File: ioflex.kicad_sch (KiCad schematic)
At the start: 2 parts, among them CN12 DF40C-50DS-0.4V, CN13 DF40C-50DS-0.4V

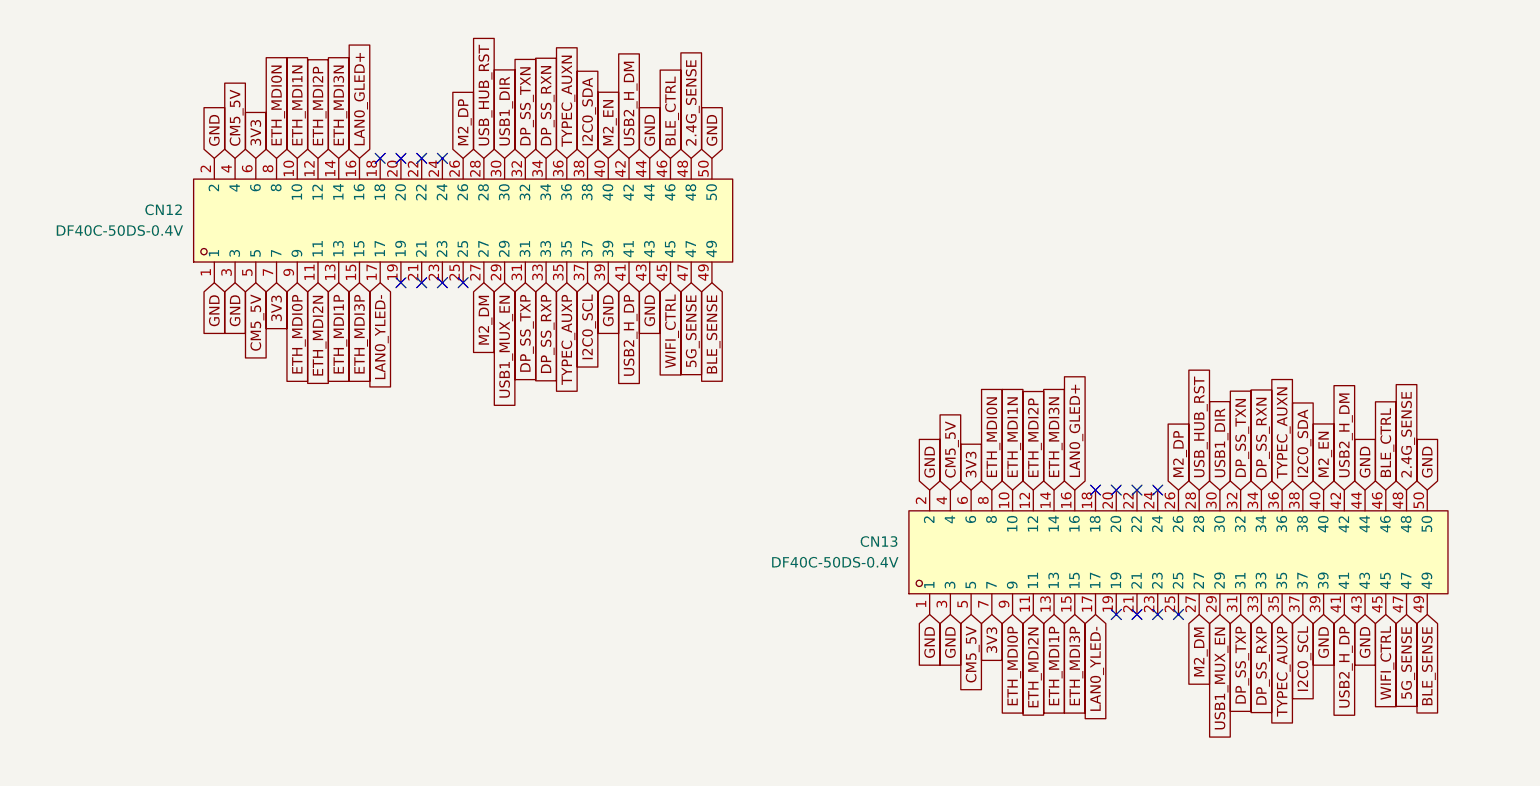
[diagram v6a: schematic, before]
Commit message: imported footprints and 3d models, replaced obsolete components, finished schematic audit, wired new usb hub and flash chip + more, removed stale nets
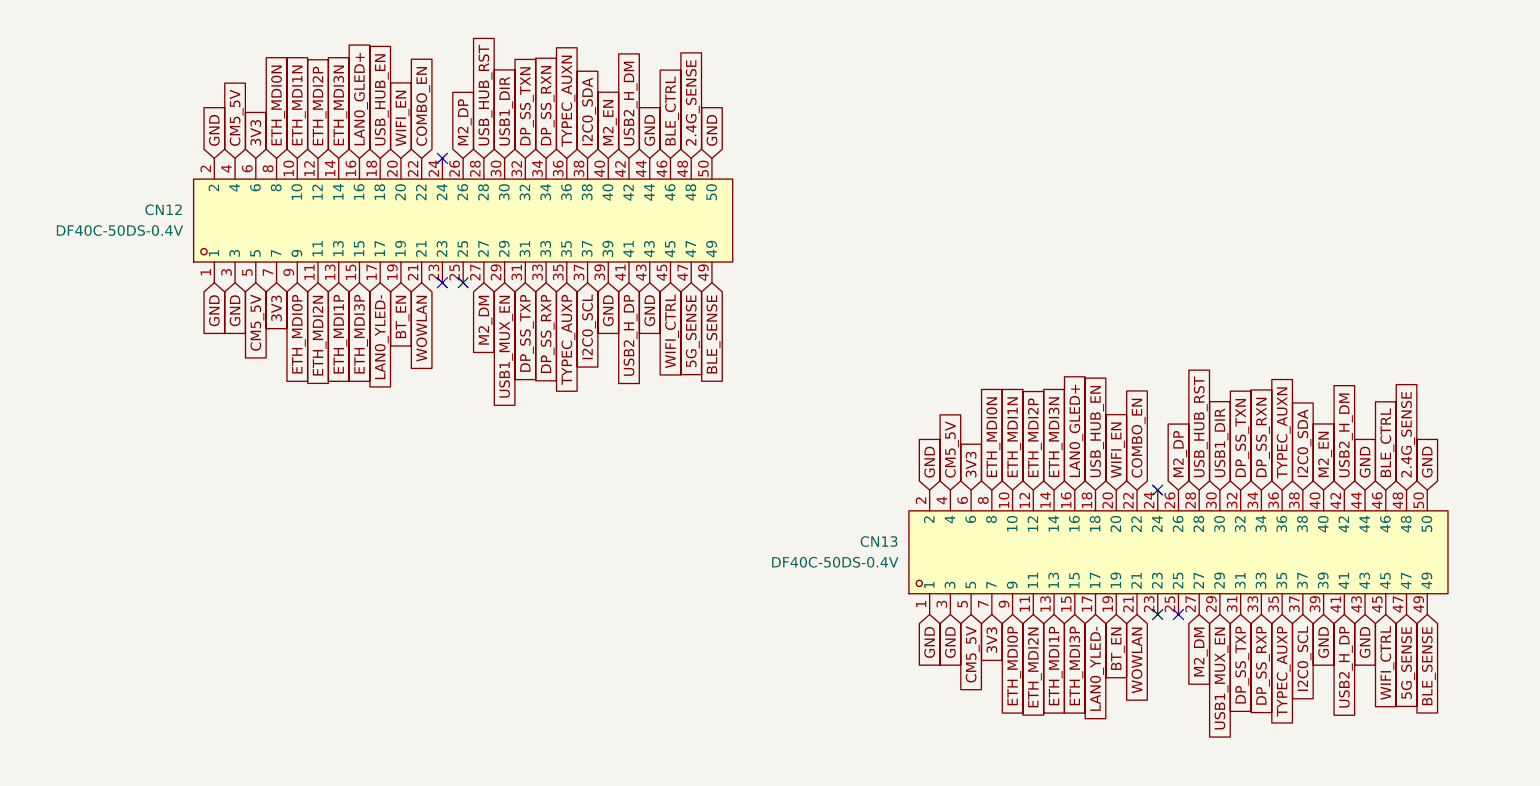
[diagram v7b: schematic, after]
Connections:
- net USB_HUB_EN: now reaches CN13.18
- net USB_HUB_EN: now also CN12.18
- net BT_EN: now reaches CN13.19
- net BT_EN: now also CN12.19
- net WIFI_EN: now reaches CN13.20
- net WIFI_EN: now also CN12.20
- net WOWLAN: now reaches CN13.21
- net WOWLAN: now also CN12.21
- net COMBO_EN: now reaches CN13.22
- net COMBO_EN: now also CN12.22
- no-connect marks 16 -> 6
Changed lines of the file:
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@@
 	(paper "A5")
 	(no_connect
-		(at 60.96 29.21)
-	)
-	(no_connect
-		(at 148.59 85.09)
-	)
-	(no_connect
-		(at 60.96 44.45)
-	)
-	(no_connect
-		(at 55.88 29.21)
-	)
-	(no_connect
 		(at 153.67 85.09)
 	)
@@
 	)
 	(no_connect
-		(at 58.42 29.21)
+		(at 63.5 29.21)
 	)
 	(no_connect
-		(at 146.05 69.85)
+		(at 151.13 85.09)
 	)
 	(no_connect
-		(at 63.5 29.21)
-	)
-	(no_connect
-		(at 146.05 85.09)
-	)
-	(no_connect
-		(at 148.59 69.85)
-	)
-	(no_connect
-		(at 58.42 44.45)
+		(at 66.04 44.45)
 	)
 	(no_connect
 		(at 63.5 44.45)
 	)
-	(no_connect
-		(at 143.51 69.85)
-	)
-	(no_connect
-		(at 66.04 44.45)
-	)
-	(no_connect
-		(at 151.13 85.09)
-	)
 	(global_label "3V3"
 		(shape input)
@@
 		)
 	)
+	(global_label "USB_HUB_EN"
+		(shape input)
+		(at 143.51 69.85 90)
+		(fields_autoplaced yes)
+		(effects
+			(font
+				(size 1.27 1.27)
+			)
+			(justify left)
+		)
+		(property "Intersheetrefs" "${INTERSHEET_REFS}"
+			(at 143.51 54.7091 90)
+			(hide yes)
+			(show_name no)
+			(do_not_autoplace no)
+			(effects
+				(font
+					(size 1.27 1.27)
+				)
+				(justify left)
+			)
+		)
+	)
 	(global_label "DP_SS_RXP"
 		(shape input)
@@
 		)
 	)
+	(global_label "WIFI_EN"
+		(shape input)
+		(at 58.42 29.21 90)
+		(fields_autoplaced yes)
+		(effects
+			(font
+				(size 1.27 1.27)
+			)
+			(justify left)
+		)
+		(property "Intersheetrefs" "${INTERSHEET_REFS}"
+			(at 58.42 19.0281 90)
+			(hide yes)
+			(show_name no)
+			(do_not_autoplace no)
+			(effects
+				(font
+					(size 1.27 1.27)
+				)
+				(justify left)
+			)
+		)
+	)
 	(global_label "ETH_MDI3N"
 		(shape input)
@@
 		)
 	)
+	(global_label "COMBO_EN"
+		(shape input)
+		(at 148.59 69.85 90)
+		(fields_autoplaced yes)
+		(effects
+			(font
+				(size 1.27 1.27)
+			)
+			(justify left)
+		)
+		(property "Intersheetrefs" "${INTERSHEET_REFS}"
+			(at 148.59 56.7653 90)
+			(hide yes)
+			(show_name no)
+			(do_not_autoplace no)
+			(effects
+				(font
+					(size 1.27 1.27)
+				)
+				(justify left)
+			)
+		)
+	)
 	(global_label "M2_DP"
 		(shape input)
@@
 		)
 	)
+	(global_label "USB_HUB_EN"
+		(shape input)
+		(at 55.88 29.21 90)
+		(fields_autoplaced yes)
+		(effects
+			(font
+				(size 1.27 1.27)
+			)
+			(justify left)
+		)
+		(property "Intersheetrefs" "${INTERSHEET_REFS}"
+			(at 55.88 14.0691 90)
+			(hide yes)
+			(show_name no)
+			(do_not_autoplace no)
+			(effects
+				(font
+					(size 1.27 1.27)
+				)
+				(justify left)
+			)
+		)
+	)
 	(global_label "ETH_MDI0P"
 		(shape input)
@@
 		)
 	)
+	(global_label "BT_EN"
+		(shape input)
+		(at 146.05 85.09 270)
+		(fields_autoplaced yes)
+		(effects
+			(font
+				(size 1.27 1.27)
+			)
+			(justify right)
+		)
+		(property "Intersheetrefs" "${INTERSHEET_REFS}"
+			(at 146.05 93.7599 90)
+			(hide yes)
+			(show_name no)
+			(do_not_autoplace no)
+			(effects
+				(font
+					(size 1.27 1.27)
+				)
+				(justify right)
+			)
+		)
+	)
 	(global_label "I2C0_SCL"
 		(shape input)
@@
 		)
 	)
+	(global_label "COMBO_EN"
+		(shape input)
+		(at 60.96 29.21 90)
+		(fields_autoplaced yes)
+		(effects
+			(font
+				(size 1.27 1.27)
+			)
+			(justify left)
+		)
+		(property "Intersheetrefs" "${INTERSHEET_REFS}"
+			(at 60.96 16.1253 90)
+			(hide yes)
+			(show_name no)
+			(do_not_autoplace no)
+			(effects
+				(font
+					(size 1.27 1.27)
+				)
+				(justify left)
+			)
+		)
+	)
 	(global_label "ETH_MDI0N"
 		(shape input)
@@
 		)
 	)
+	(global_label "WIFI_EN"
+		(shape input)
+		(at 146.05 69.85 90)
+		(fields_autoplaced yes)
+		(effects
+			(font
+				(size 1.27 1.27)
+			)
+			(justify left)
+		)
+		(property "Intersheetrefs" "${INTERSHEET_REFS}"
+			(at 146.05 59.6681 90)
+			(hide yes)
+			(show_name no)
+			(do_not_autoplace no)
+			(effects
+				(font
+					(size 1.27 1.27)
+				)
+				(justify left)
+			)
+		)
+	)
 	(global_label "USB1_DIR"
 		(shape input)
@@
 		)
 	)
+	(global_label "WOWLAN"
+		(shape input)
+		(at 60.96 44.45 270)
+		(fields_autoplaced yes)
+		(effects
+			(font
+				(size 1.27 1.27)
+			)
+			(justify right)
+		)
+		(property "Intersheetrefs" "${INTERSHEET_REFS}"
+			(at 60.96 55.1157 90)
+			(hide yes)
+			(show_name no)
+			(do_not_autoplace no)
+			(effects
+				(font
+					(size 1.27 1.27)
+				)
+				(justify right)
+			)
+		)
+	)
 	(global_label "ETH_MDI3P"
 		(shape input)
@@
 		)
 	)
+	(global_label "WOWLAN"
+		(shape input)
+		(at 148.59 85.09 270)
+		(fields_autoplaced yes)
+		(effects
+			(font
+				(size 1.27 1.27)
+			)
+			(justify right)
+		)
+		(property "Intersheetrefs" "${INTERSHEET_REFS}"
+			(at 148.59 95.7557 90)
+			(hide yes)
+			(show_name no)
+			(do_not_autoplace no)
+			(effects
+				(font
+					(size 1.27 1.27)
+				)
+				(justify right)
+			)
+		)
+	)
 	(global_label "CM5_5V"
 		(shape input)
@@
 			)
 		)
+	)
+	(global_label "BT_EN"
+		(shape input)
+		(at 58.42 44.45 270)
+		(fields_autoplaced yes)
+		(effects
+			(font
+				(size 1.27 1.27)
+			)
+			(justify right)
+		)
+		(property "Intersheetrefs" "${INTERSHEET_REFS}"
+			(at 58.42 53.1199 90)
+			(hide yes)
+			(show_name no)
+			(do_not_autoplace no)
+			(effects
+				(font
+					(size 1.27 1.27)
+				)
+				(justify right)
+			)
+		)
